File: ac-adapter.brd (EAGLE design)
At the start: 113 x 52.7 mm, 88 parts, among them IC1 SSC3S900, IC2 TL431, Q1 300V 5A, Q2 300V 5A, Q3 TLP621-1, T1 COMMON_FILTER-SU10VFC, T2 TRANSFORMAER_FLYBACK-ETD34

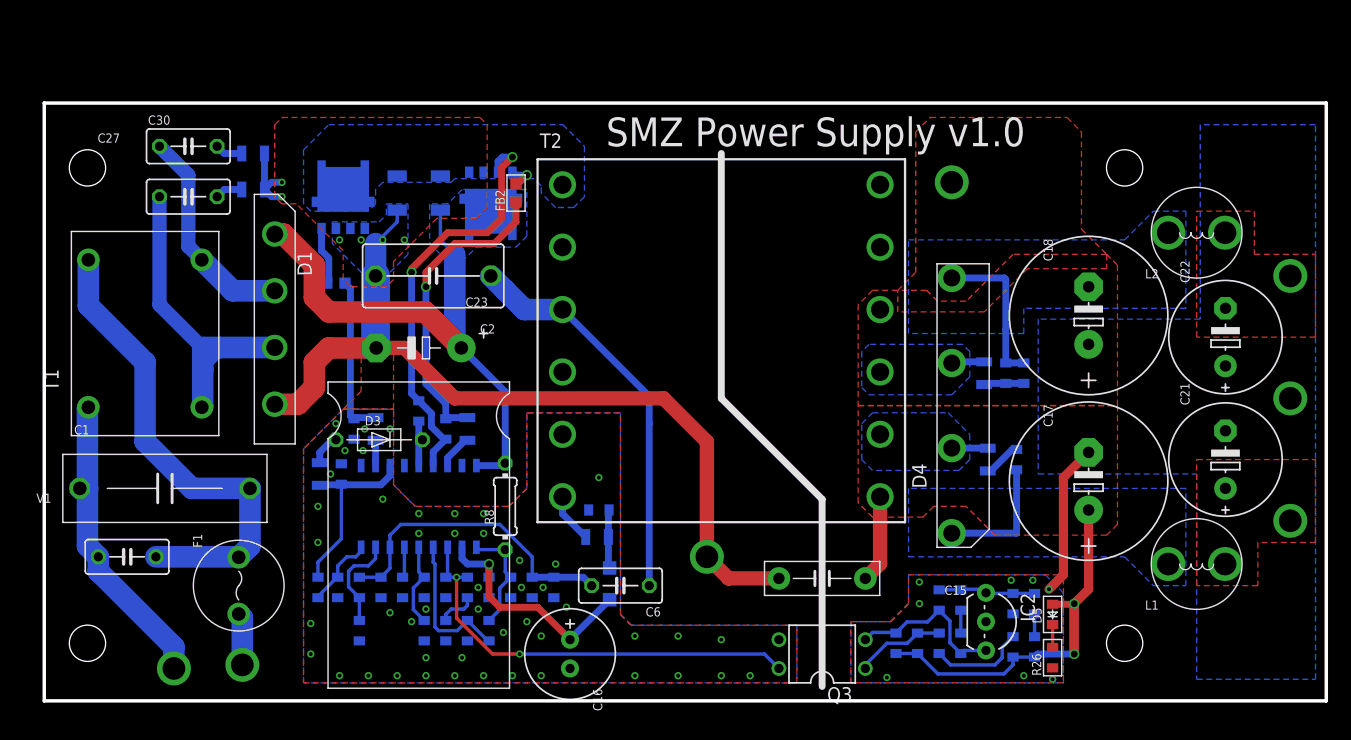
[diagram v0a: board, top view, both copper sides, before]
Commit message: UCC256404Aに変更
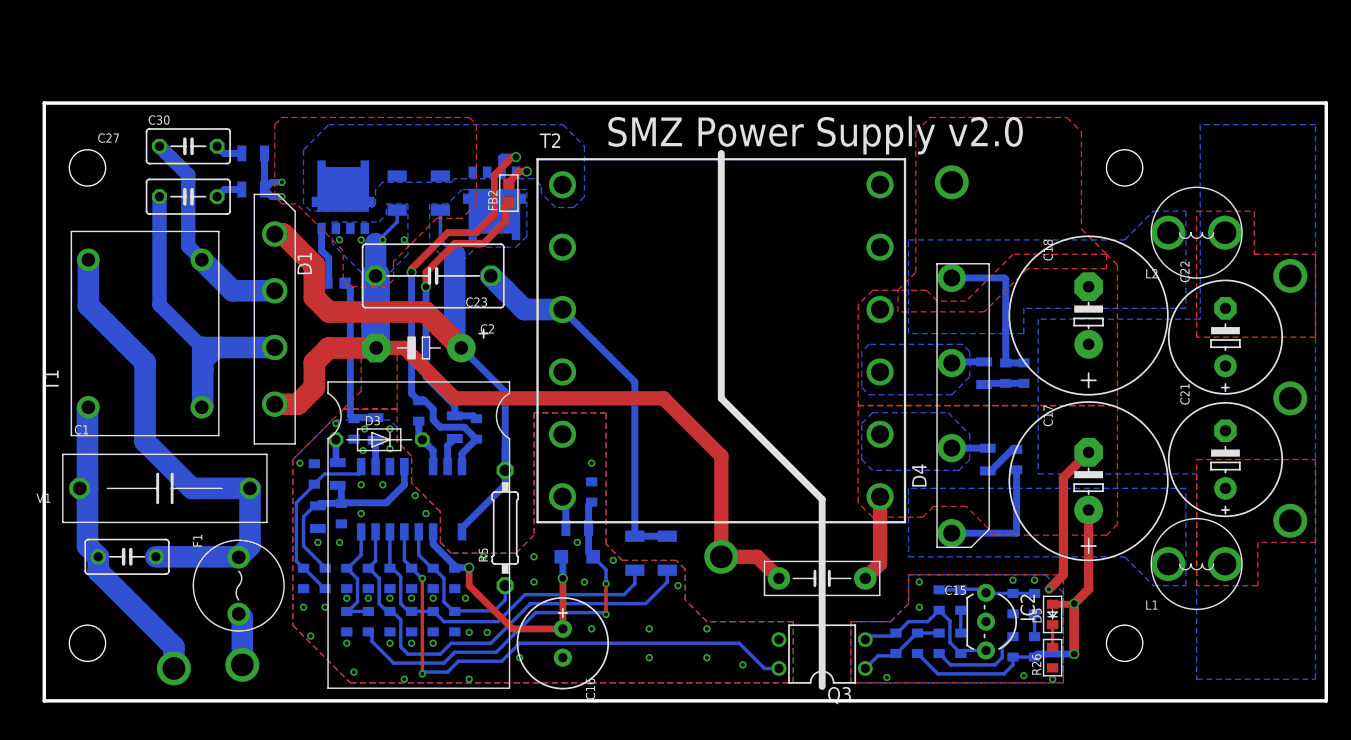
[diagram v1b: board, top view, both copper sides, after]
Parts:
- removed R25: DNP, my_rcl:1608
- removed R27: 100k, my_rcl:1608
- added C31: 470p, my_rcl:1608
- added C32: 10u, my_rcl:2012
- C10: value 0.22u -> 10p
- C11: value 10000p -> DNP
- C12: value DNP -> 100p
- C14: value 1000p -> 10p
- C24: value 0.1u -> 10n
- C25: value 0.1u -> 1u
- C26: value 0.1u -> DNP
- C28: value 1000p -> DNP
- C5: value 0.01u -> 1u
- C6: device my_rcl:C050 -> my_rcl:3225
- C7: value 0.22u -> 1kV 47p; device my_rcl:1608 -> my_rcl:3225
- C8: value 0.47u -> 3.3n
- IC1: value SSC3S900 -> UCC256404A; device my_ic:SOP18 -> my_ic:SO16-LACK3-13
- R11: value 10k -> 15k
- R12: value 1.5k -> DNP
- R22: value 10k -> 3.3k
- R23: value DNP -> 47
- R5: value 100k -> 1M; device my_rcl:1608 -> my_rcl:0207/10
- R7: value 100k -> 240k
- R8: value 1M -> 240k; device my_rcl:0204/7 -> my_rcl:1608
- R9: value 39 -> DNP
- moved C7 23.5 mm to (54.9, 13.0)
- moved R8 18.9 mm to (22.9, 10.8), flipped to the bottom
- moved R5 11.5 mm to (40.6, 15.2), flipped to the top
- moved R23 11.1 mm to (34.3, 6.99)
- moved R9 11.1 mm to (32.4, 6.99)
- moved C26 11.1 mm to (30.5, 6.99)
- moved R11 10.7 mm to (28.6, 6.99), turned to 270 degrees
- moved R22 10.7 mm to (26.7, 6.99)
- moved C5 10.2 mm to (23.8, 20.0), turned to 90 degrees
- moved C10 6.74 mm to (30.5, 10.8)
- moved R7 5.50 mm to (24.8, 10.8)
- moved C8 4.98 mm to (28.6, 10.8)
- moved D2 3.72 mm to (47.0, 12.7), turned to 0 degrees
- moved C4 3.49 mm to (26.2, 16.5), turned to 270 degrees
- moved R6 3.21 mm to (36.2, 6.99)
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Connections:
- removed net N$19: C7.1, IC1.6
- removed net N$20: C8.1, IC1.5, R5.2
- removed net N$21: C10.1, R6.1
- removed net N$25: C12.1, IC1.3, Q3.4, R6.2
- removed net N$27: C14.1, C6.2, IC1.7, R23.2, R25.1, R9.2
- removed net N$28: IC1.4, R11.1, R22.2
- removed net N$31: C26.1, IC1.1, R11.2, R8.1
- removed net VCC: C16.+, C25.1, D2.2, IC1.2
- new net UCC_BW: C14.1, IC1.8, R11.1, R22.2
- new net UCC_FB: C12.1, IC1.5, Q3.4
- new net UCC_ISNS: C10.1, C6.2, IC1.6, R23.2, R9.2
- new net UCC_VCC: C16.+, C25.1, D2.2, IC1.3
- new net UCC_VCR: C26.1, C7.2, C8.1, IC1.7
- net N$12: now also IC1.10; no longer IC1.11
- net N$13: now also IC1.15; no longer IC1.16
- net N$16: now also C32.1, R7.2; no longer R27.2
- net N$17: now also R7.1, R8.2; no longer R27.1
- net N$18: now also C31.1, IC1.4, R5.1, R6.2; no longer IC1.8, R25.2, R7.2
- net N$24: now also R11.2
- net N$34: now also R18.2
- net N$40: no longer R18.2
- net N$8: now also C7.1
- net PGND: now also C31.2, C32.2, IC1.11, R6.1, R8.1; no longer C7.2, IC1.10, R5.1, R7.1
- net SW: now also IC1.16; no longer IC1.15
- net VH: now also IC1.1, R5.2; no longer IC1.18, R8.2
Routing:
- net UCC_FB: track 0.00 -> 46.7 mm, vias 0 -> 2
- net UCC_VCR: track 0.00 -> 39.3 mm
- net N$25: track 38.5 -> 0.00 mm, vias 2 -> 0
- net UCC_ISNS: track 0.00 -> 30.7 mm
- net N$24: track 5.18 -> 35.0 mm, vias 0 -> 2
- net N$27: track 27.4 -> 0.00 mm
- net UCC_VCC: track 0.00 -> 23.1 mm, vias 0 -> 2
- net VCC: track 21.3 -> 0.00 mm, vias 1 -> 0
- net N$28: track 13.1 -> 0.00 mm
- net UCC_BW: track 0.00 -> 10.4 mm
- net N$31: track 9.86 -> 0.00 mm
- net N$17: track 6.52 -> 16.0 mm
- net N$20: track 7.44 -> 0.00 mm
- net VH: track 49.6 -> 56.5 mm
- net N$18: track 8.58 -> 14.6 mm
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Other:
- board text added: "SMZ Power Supply v2.0"
- board text removed: "SMZ Power Supply v1.0"

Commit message: GaN
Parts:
- added D6, D7: SBD, my_rcl:SOD123
- Q1, Q2: device my_ic:DFN5_5X6 -> my_ic:PQFN8X8
- moved FB1 13.3 mm to (21.9, 49.5), turned to 180 degrees
- moved C13 3.84 mm to (27.6, 46.4), flipped to the top
- moved FB2 3.62 mm to (40.0, 41.3), turned to 0 degrees
- moved Q2 3.01 mm to (25.4, 47.3)
- moved Q1 2.56 mm to (39.4, 41.3)
- moved D1 2.54 mm to (17.8, 33.7)
- moved C29 2.03 mm to (33.7, 43.2)
- moved T1 1.27 mm to (7.62, 32.4)
- moved C27 1.27 mm to (11.4, 44.5)
- moved C30 1.27 mm to (11.4, 48.9)
- moved R28 1.27 mm to (17.1, 45.1)
- moved R29 1.27 mm to (17.1, 48.3)
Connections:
- net N$39: now also Q2.G; no longer Q2.4
- net N$41: now also Q1.G; no longer Q1.4
- net PGND: now also D7.1, Q2.S; no longer Q2.1, Q2.2, Q2.3
- net SW: now also D6.1, D7.2, Q1.S, Q2.D; no longer Q1.1, Q1.2, Q1.3, Q2.5_6, Q2.5_6_1, Q2.5_6_2, Q2.5_6_3, Q2.5_6_4
- net VH: now also D6.2, Q1.D; no longer Q1.5_6, Q1.5_6_1, Q1.5_6_2, Q1.5_6_3, Q1.5_6_4
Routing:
- net N$9: track 14.3 -> 29.3 mm
- net SW: track 39.8 -> 32.6 mm, vias 2 -> 6
- net PGND: track 81.2 -> 77.1 mm, vias 52 -> 57
- net N$2: track 26.4 -> 22.7 mm
- net N$39: track 5.16 -> 2.45 mm
- net N$5: track 19.1 -> 17.8 mm
- net N$41: track 3.11 -> 3.70 mm
- net N$26: track 42.9 -> 43.4 mm
- added copper zone on layer 1, net SW
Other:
- board text added: "SMZ Power Supply v2.1"
- board text removed: "SMZ Power Supply v2.0"

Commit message: 値修正
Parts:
- C6: value 1kV 470p -> 220p 1kV
- C7: value 1kV 47p -> 100p 1kV
- C8: value 3.3n -> 6.8n
- R1, R2: value 10 -> 120
- R17, R18: value 10k -> 1.5k
- R23: value 47 -> 120
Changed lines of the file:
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@@
 <attribute name="VALUE" x="78.486" y="4.5085" size="0.8128" layer="27" font="vector" ratio="15" rot="R180"/>
 </element>
-<element name="R1" library="my_rcl" package="2012" value="10" x="36.195" y="24.13" smashed="yes" rot="MR90">
+<element name="R1" library="my_rcl" package="2012" value="120" x="36.195" y="24.13" smashed="yes" rot="MR90">
 <attribute name="NAME" x="34.195" y="22.73" size="0.8128" layer="26" rot="MR90"/>
 <attribute name="VALUE" x="35.27125" y="27.175" size="0.8128" layer="28" font="vector" ratio="15" rot="MR180"/>
 </element>
-<element name="R2" library="my_rcl" package="2012" value="10" x="29.21" y="23.97125" smashed="yes" rot="MR270">
+<element name="R2" library="my_rcl" package="2012" value="120" x="29.21" y="23.97125" smashed="yes" rot="MR270">
 <attribute name="NAME" x="31.21" y="25.37125" size="0.8128" layer="26" rot="MR270"/>
 <attribute name="VALUE" x="28.60375" y="27.01625" size="0.8128" layer="28" font="vector" ratio="15" rot="MR180"/>
@@
 <attribute name="VALUE" x="87.68375" y="3.02875" size="0.8128" layer="28" font="vector" ratio="15" rot="MR270"/>
 </element>
-<element name="R17" library="my_rcl" package="1608" value="10k" x="76.99375" y="5.08" smashed="yes" rot="MR90">
+<element name="R17" library="my_rcl" package="1608" value="1.5k" x="76.99375" y="5.08" smashed="yes" rot="MR90">
 <attribute name="NAME" x="77.99375" y="3.48" size="0.8128" layer="26" rot="MR90"/>
 <attribute name="VALUE" x="77.52375" y="3.1875" size="0.8128" layer="28" font="vector" ratio="15" rot="MR270"/>
@@
 <attribute name="VALUE" x="25.705" y="27.04125" size="0.8128" layer="28" font="vector" ratio="15" rot="MR180"/>
 </element>
-<element name="C6" library="my_rcl" package="3225" value="1kV 470p" x="52.07" y="13.0175" smashed="yes" rot="MR270">
+<element name="C6" library="my_rcl" package="3225" value="220p 1kV" x="52.07" y="13.0175" smashed="yes" rot="MR270">
 <attribute name="NAME" x="50.165" y="16.5735" size="0.8128" layer="26" ratio="10" rot="MR270"/>
 <attribute name="VALUE" x="52.41925" y="10.2235" size="0.8128" layer="28" font="vector" ratio="15" rot="MR270"/>
@@
 <attribute name="VALUE" x="79.27" y="3.1875" size="0.8128" layer="28" font="vector" ratio="15" rot="MR270"/>
 </element>
-<element name="R18" library="my_rcl" package="1608" value="10k" x="75.08875" y="5.08" smashed="yes" rot="MR270">
+<element name="R18" library="my_rcl" package="1608" value="1.5k" x="75.08875" y="5.08" smashed="yes" rot="MR270">
 <attribute name="NAME" x="74.08875" y="6.68" size="0.8128" layer="26" rot="MR270"/>
 <attribute name="VALUE" x="75.61875" y="3.1875" size="0.8128" layer="28" font="vector" ratio="15" rot="MR270"/>
@@
 <attribute name="VALUE" x="20.7425" y="19.0375" size="0.8128" layer="28" font="vector" ratio="15" rot="MR90"/>
 </element>
-<element name="C7" library="my_rcl" package="3225" value="1kV 47p" x="54.9275" y="13.0175" smashed="yes" rot="MR270">
+<element name="C7" library="my_rcl" package="3225" value="100p 1kV" x="54.9275" y="13.0175" smashed="yes" rot="MR270">
 <attribute name="NAME" x="53.0225" y="16.5735" size="0.8128" layer="26" ratio="10" rot="MR270"/>
 <attribute name="VALUE" x="55.27675" y="10.2235" size="0.8128" layer="28" font="vector" ratio="15" rot="MR270"/>
 </element>
-<element name="C8" library="my_rcl" package="1608" value="3.3n" x="28.575" y="10.795" smashed="yes" rot="MR270">
+<element name="C8" library="my_rcl" package="1608" value="6.8n" x="28.575" y="10.795" smashed="yes" rot="MR270">
 <attribute name="NAME" x="27.575" y="12.395" size="0.8128" layer="26" rot="MR270"/>
 <attribute name="VALUE" x="26.34" y="4.975" size="0.8128" layer="28" font="vector" ratio="15" rot="MR180"/>
@@
 <attribute name="VALUE" x="29.03875" y="3.705" size="0.8128" layer="28" font="vector" ratio="15" rot="MR180"/>
 </element>
-<element name="R23" library="my_rcl" package="1608" value="47" x="34.29" y="6.985" smashed="yes" rot="MR90">
+<element name="R23" library="my_rcl" package="1608" value="120" x="34.29" y="6.985" smashed="yes" rot="MR90">
 <attribute name="NAME" x="35.29" y="5.385" size="0.8128" layer="26" rot="MR90"/>
 <attribute name="VALUE" x="34.9125" y="3.705" size="0.8128" layer="28" font="vector" ratio="15" rot="MR180"/>

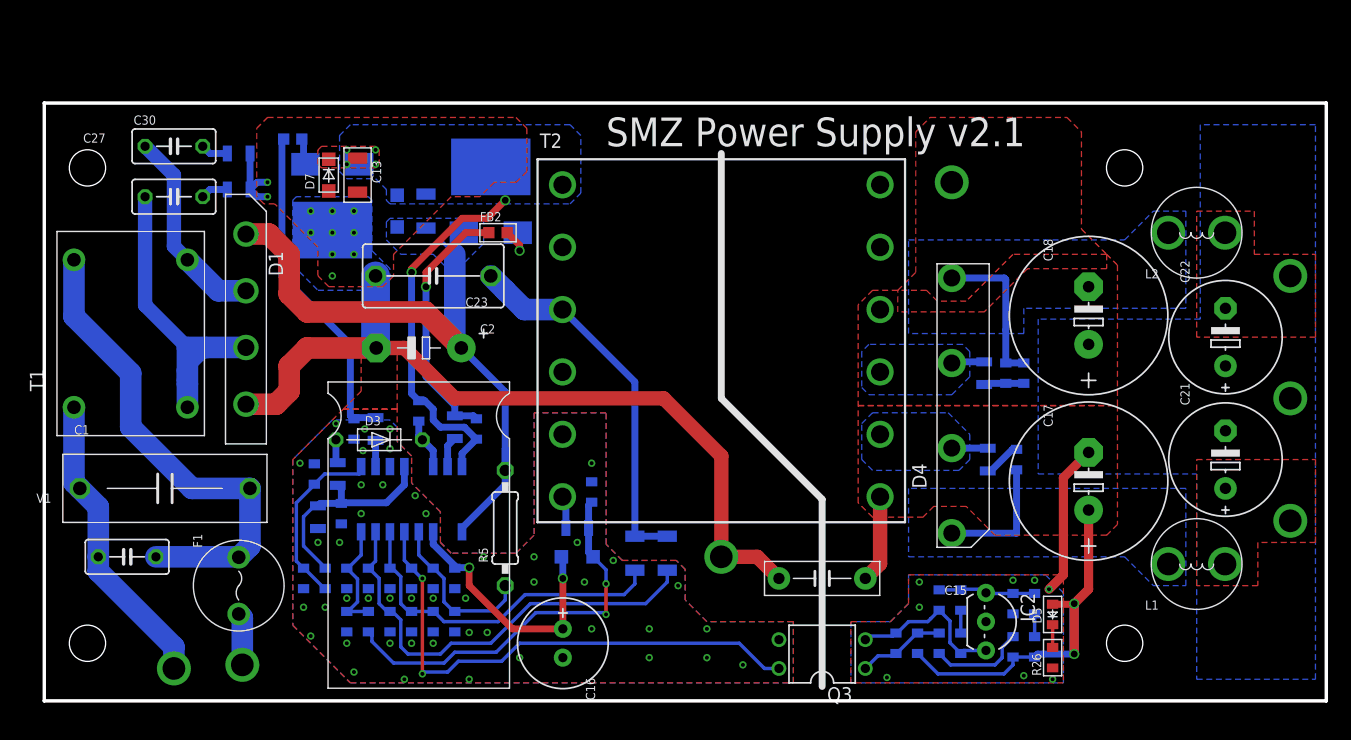
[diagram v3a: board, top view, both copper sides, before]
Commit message: ver2.3 GaNとSiを共通に
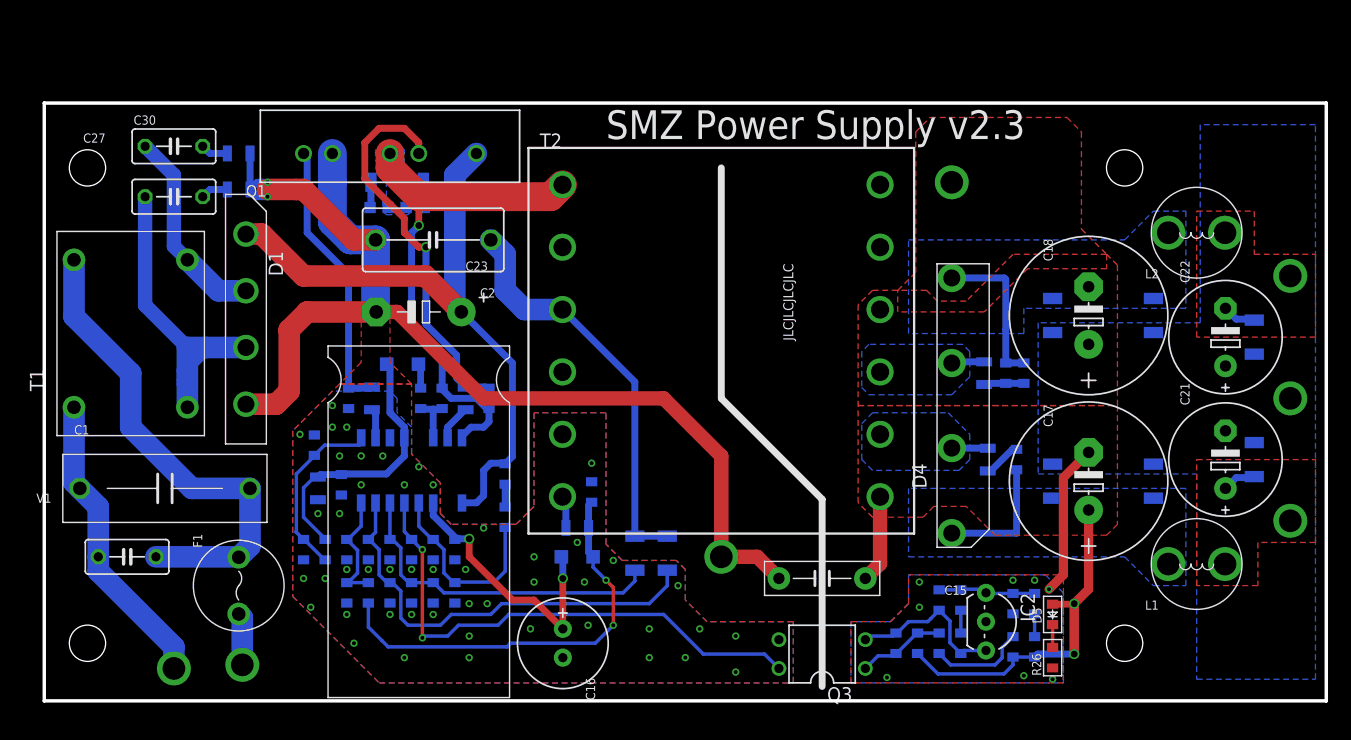
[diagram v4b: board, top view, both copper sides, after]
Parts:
- removed D6, D7: SBD, my_rcl:SOD123
- removed Q2: 300V 5A, my_ic:PQFN8X8
- added C33, C34, C35, C36, C37, C38: 10u, my_rcl:3225-2
- added R25: 240k, my_rcl:1608
- C12: value 100p -> 22p
- C2: device my_rcl:E5-16A2 -> my_rcl:E5-16A3
- D3: device my_rcl:D0204/7 -> my_rcl:SOD123
- Q1: value 300V 5A -> 200V 3A; device my_ic:PQFN8X8 -> my_ic:NMOS-FET_HALF
- R3: value 10 -> 39; device my_rcl:2012 -> my_rcl:1608
- R5: value 1M -> 240k; device my_rcl:0207/10 -> my_rcl:1608
- R6: value 10k -> 6.8k
- moved Q1 11.3 mm to (30.5, 48.3), flipped to the top
- moved R3 9.89 mm to (33.2, 26.7)
- moved FB1 9.72 mm to (29.5, 43.5), turned to 0 degrees
- moved FB2 7.63 mm to (32.7, 43.5), flipped to the bottom
- moved D3 6.98 mm to (31.6, 29.7), flipped to the bottom, turned to 180 degrees
- moved R5 4.76 mm to (40.6, 20.0), flipped to the bottom
- moved C2 3.18 mm to (33.0, 34.3)
- moved C23 3.17 mm to (34.3, 40.6)
- moved R20 2.92 mm to (39.2, 26.7)
- moved C29 2.84 mm to (34.9, 45.7), turned to 0 degrees
- moved R21 2.74 mm to (26.8, 26.7)
- moved R2 2.72 mm to (28.9, 26.7)
- moved R1 2.71 mm to (37.1, 26.7)
- moved C32 2.54 mm to (24.1, 18.7)
- moved C10 2.54 mm to (30.5, 13.3)
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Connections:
- removed net N$39: FB1.2, Q2.G
- removed net N$41: FB2.2, Q1.G
- new net N$13: C13.1, FB1.2
- new net N$19: C29.2, FB2.1
- new net N$21: R25.2, R5.1
- net GND: now also C33.2, C34.1, C35.2, C36.1, C37.2, C38.1
- net N$14: now also R3.1; no longer D3.2
- net N$15: now also D3.2; no longer D3.1
- net N$16: now also D3.1; no longer R3.1
- net N$18: now also R25.1; no longer R5.1
- net N$2: now also Q1.GT; no longer FB2.1
- net N$40: now also C33.1, C37.1
- net N$7: now also C34.2, C38.2
- net N$9: now also Q1.GB; no longer FB1.1
- net PGND: now also Q1.V-; no longer D7.1, Q2.S
- net SW: now also FB1.1, FB2.2, Q1.SW; no longer C13.1, C29.2, D6.1, D7.2, Q1.S, Q2.D
- net V+: now also C35.1
- net V-: now also C36.2
- net VH: now also Q1.V+; no longer D6.2, Q1.D
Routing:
- net PGND: track 77.1 -> 105.2 mm, vias 57 -> 50
- net SW: track 32.6 -> 45.4 mm, vias 6 -> 1
- net N$2: track 22.7 -> 34.5 mm
- net N$16: track 18.7 -> 24.1 mm
- net N$9: track 29.3 -> 24.4 mm
- net N$41: track 3.70 -> 0.00 mm, vias 1 -> 0
- net N$8: track 33.0 -> 36.2 mm
- net V-: track 0.00 -> 2.97 mm
- net V+: track 0.00 -> 2.97 mm
- net VH: track 56.8 -> 59.7 mm
- net N$18: track 14.6 -> 17.2 mm
- net N$39: track 2.45 -> 0.00 mm
- net N$19: track 0.00 -> 2.25 mm
- net N$13: track 0.00 -> 2.25 mm
- net N$24: track 35.0 -> 37.1 mm
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- removed copper zone on layer 1, net SW
- removed copper zone on layer 16, net VH
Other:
- board text added: "JLCJLCJLCJLC"
- board text added: "SMZ Power Supply v2.3"
- board text removed: "SMZ Power Supply v2.1"

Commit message: 曲げる前
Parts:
- removed FB2: FB, my_rcl:1608-FB
- added C39: DNP, my_rcl:1608
- added FB3: FB-3216, my_rcl:3216-J
- added R27: Thermistor, my_rcl:THERMISTOR090
- C37, C38: value 10u -> 1u; device my_rcl:3225-2 -> my_rcl:2012-2
- FB1: value FB -> FB-1608FB
- moved FB1 7.63 mm to (36.8, 41.3), turned to 90 degrees
- moved C29 4.26 mm to (33.0, 41.9)
- moved C2 1.42 mm to (31.8, 34.9)
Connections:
- removed net N$19: C29.2, FB2.1
- new net N$25: D1.1, R27.1
- new net N$27: FB3.2, T2.1
- net N$13: now also C29.1; no longer C13.1
- net N$40: now also C39.2
- net N$6: now also C39.1
- net PGND: now also C29.2
- net SW: now also C13.1, FB3.1; no longer FB1.1, FB2.2, T2.1
- net VH: now also FB1.1, R27.2; no longer C29.1, D1.1
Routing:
- net SW: track 45.4 -> 32.6 mm
- net N$2: track 34.5 -> 25.6 mm
- net VH: track 59.7 -> 54.1 mm, vias 0 -> 3
- net N$25: track 0.00 -> 5.56 mm
- net N$27: track 0.00 -> 3.79 mm
- net PGND: track 105.2 -> 101.8 mm
- net N$19: track 2.25 -> 0.00 mm
- net N$13: track 2.25 -> 0.00 mm
- net N$6: track 2.01 -> 3.94 mm
- added copper zone on layer 16, net N$13
- added copper zone on layer 16, net VH
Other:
- board text added: "SMZ Power Supply v2.4"
- board text removed: "SMZ Power Supply v2.3"
